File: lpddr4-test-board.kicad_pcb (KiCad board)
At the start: 8 copper layers, 117 x 86 mm, 257 parts, among them IC1 TPS54561, IC3 TPD8S009DSMR, J1 0878311420, J10 61300311121, J2 08B0-1X1T-36-F, J3 DC_SOCKET, J4 WE_629105150521, J5 2309409-1, J6 685119134923, J7 1140084168, Q2 BSS138APW, Q3 BSS138APW, Q4 BSS138APW, Q5 BSS138APW, Q6 BSS138APW, Q7 BSS138APW, Q8 BSS138APW, U1 XC7K70T-FBG484, U2 ASEM1-100.000MHZ-LC-T, U3 S25FL128SAGNFI000, U4 TPS65296, U5 TPS62823DLCT, U6 DP83848JSQ_NOPB, U7 FT4232HQ, Y1 ABM8G-25.000MHZ-18-D2Y-T

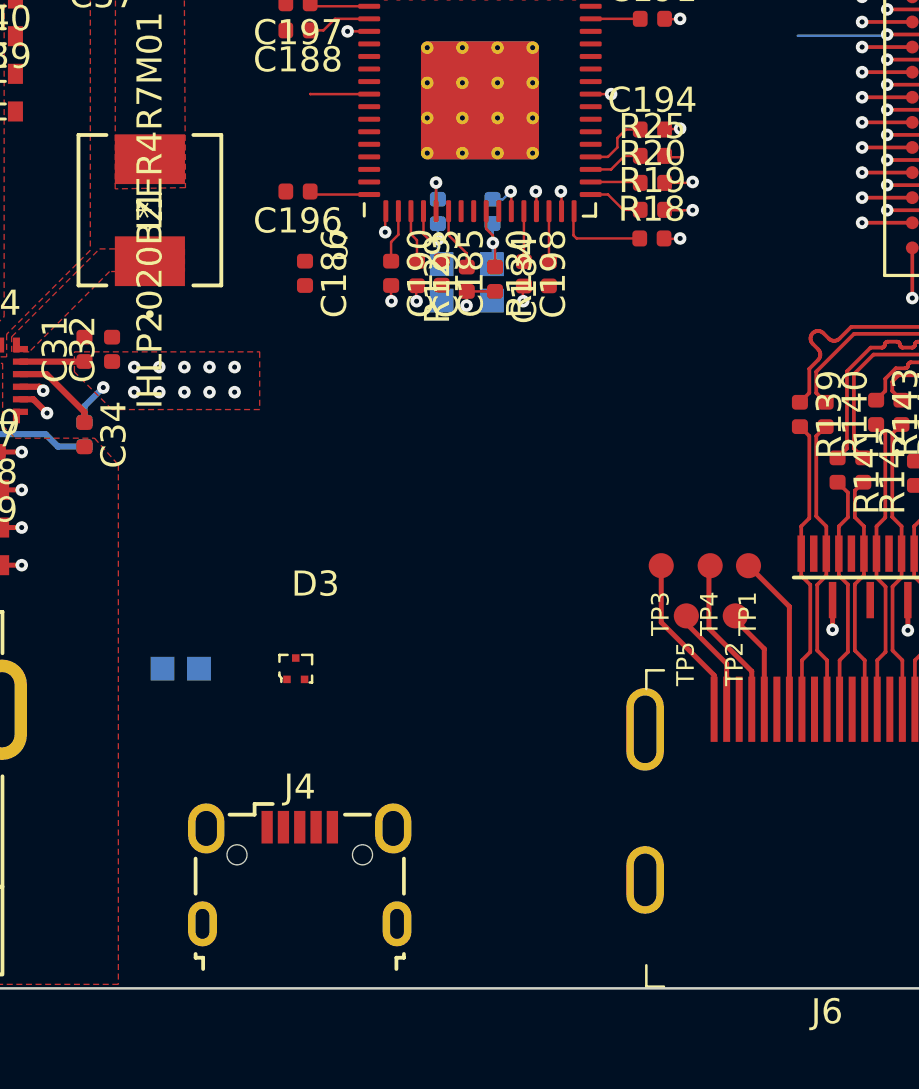
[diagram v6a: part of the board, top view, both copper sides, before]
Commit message: Add aux JTAG connection to schematics
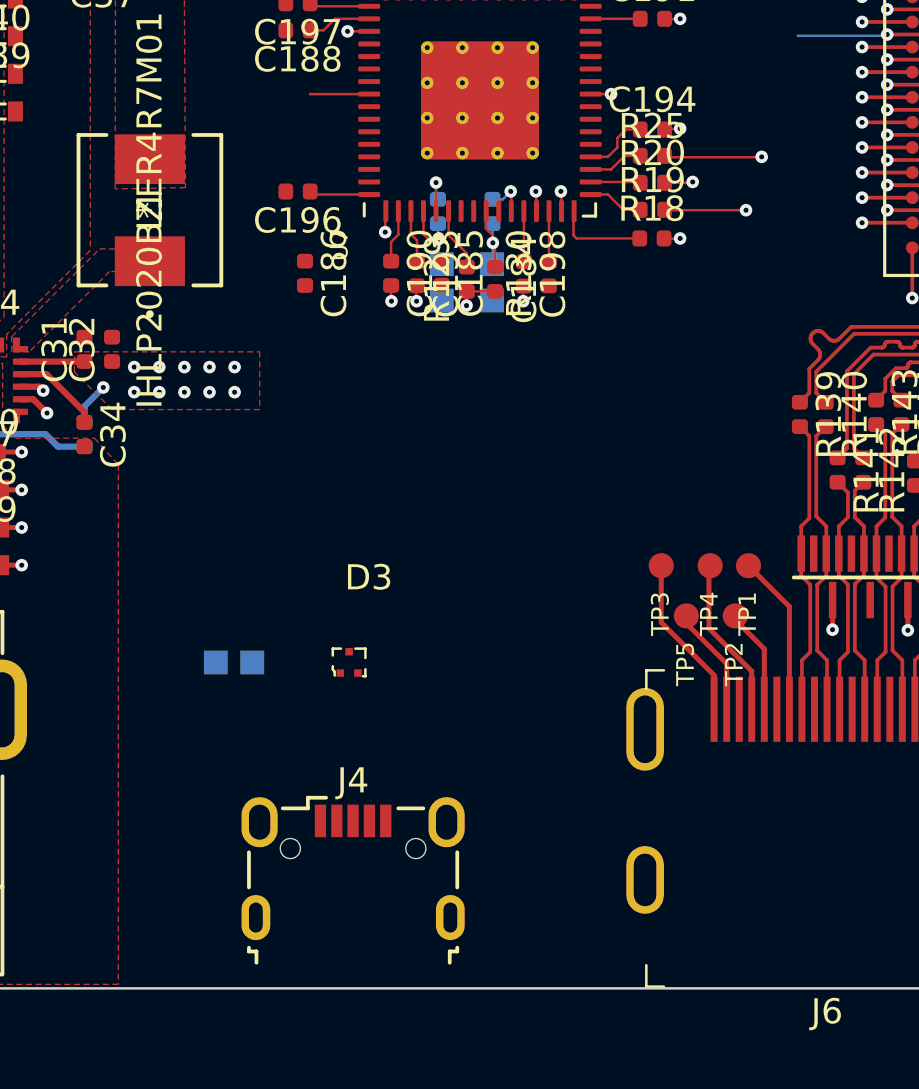
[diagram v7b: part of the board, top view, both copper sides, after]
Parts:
- moved D3 2.14 mm to (136.1, 123.0)
- moved FB6 2.14 mm to (131.5, 123.0)
- moved J4 2.14 mm to (136.3, 131.2)
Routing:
- net TCK_JTAG: track 76.5 -> 90.1 mm
- net TDI_JTAG: track 79.8 -> 90.7 mm
- net TDO_JTAG: track 80.2 -> 88.6 mm
- net TMS_JTAG: track 79.6 -> 86.7 mm
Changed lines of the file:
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@@
     (thickness 1.6)
     (drawings 130)
-    (tracks 3158)
+    (tracks 3169)
     (zones 0)
     (modules 257)
@@
   )
   (module lpddr4-test-board-footprints:0603 (layer B.Cu)
-    (at 129.389 123.264)
+    (at 131.514 123.014)
     (attr smd)
     (fp_text reference FB6 (at 0 0 90) (layer F.SilkS) hide
@@
   )
   (module lpddr4-test-board-footprints:SOT-3 (layer F.Cu)
-    (at 133.97281 123.264)
+    (at 136.09781 123.014)
     (descr http://www.ti.com/lit/ds/symlink/tpd2eusb30.pdf)
     (attr smd)
@@
   )
   (module lpddr4-test-board-footprints:USB_Micro_B_Female_629105150521 (layer F.Cu)
-    (at 134.132 131.479)
+    (at 136.257 131.229)
     (descr "USB Micro-B receptacle, http://www.mouser.com/ds/2/445/629105150521-469306.pdf")
     (tags "usb micro receptacle")
@@
   (segment (start 170.411328 90.997157) (end 171.036329 90.997156) (width 0.1) (layer In5.Cu) (net 23))
   (segment (start 168.620327 89.247157) (end 170.370327 90.997157) (width 0.1) (layer In5.Cu) (net 23))
-  (segment (start 148.786328 89.247157) (end 168.620327 89.247157) (width 0.1) (layer In5.Cu) (net 23))
   (segment (start 170.370327 90.997157) (end 170.411328 90.997157) (width 0.1) (layer In5.Cu) (net 23))
-  (segment (start 149.286328 106.122157) (end 149.286328 106.747157) (width 0.1) (layer In5.Cu) (net 23))
-  (via blind (at 149.286328 102.872157) (size 0.5) (drill 0.2) (layers GND1 In5.Cu) (net 24))
-  (segment (start 148.661328 102.887157) (end 149.271328 102.887157) (width 0.1) (layer F.Cu) (net 24))
+  (segment (start 157.536328 89.247157) (end 156.036328 89.247157) (width 0.1) (layer In5.Cu) (net 23))
+  (segment (start 157.536328 89.247157) (end 168.620327 89.247157) (width 0.1) (layer In5.Cu) (net 23))
+  (segment (start 156.036328 89.247157) (end 153.161328 92.122157) (width 0.1) (layer In5.Cu) (net 23))
+  (segment (start 153.161328 92.122157) (end 153.161328 104.997157) (width 0.1) (layer In5.Cu) (net 23))
+  (segment (start 149.286328 106.122157) (end 152.036328 106.122157) (width 0.1) (layer In5.Cu) (net 23))
+  (segment (start 153.161328 104.997157) (end 152.036328 106.122157) (width 0.1) (layer In5.Cu) (net 23))
+  (segment (start 157.286328 89.247157) (end 157.536328 89.247157) (width 0.1) (layer In5.Cu) (net 23))
   (segment (start 169.536329 90.497157) (end 170.036329 89.997157) (width 0.15) (layer F.Cu) (net 24))
   (via blind (at 170.036329 89.997157) (size 0.5) (drill 0.2) (layers F.Cu In5.Cu) (net 24) (status 40000))
@@
   (segment (start 206.278 72.273) (end 203.323 72.273) (width 0.15) (layer F.Cu) (net 24))
   (segment (start 195.981 77.123) (end 201.95 77.123) (width 0.1) (layer In2.Cu) (net 24))
-  (segment (start 149.286328 105.372157) (end 149.286328 102.872157) (width 0.1) (layer In5.Cu) (net 24))
-  (segment (start 169.036328 88.997157) (end 148.598828 88.997157) (width 0.1) (layer In5.Cu) (net 24))
-  (segment (start 149.786328 105.872157) (end 149.286328 105.372157) (width 0.1) (layer In5.Cu) (net 24))
+  (segment (start 148.661328 102.887157) (end 152.521328 102.887157) (width 0.1) (layer F.Cu) (net 24))
+  (via blind (at 152.536328 102.872157) (size 0.5) (drill 0.2) (layers F.Cu In5.Cu) (net 24))
+  (segment (start 152.521328 102.887157) (end 152.536328 102.872157) (width 0.1) (layer F.Cu) (net 24))
+  (segment (start 152.911328 91.997157) (end 152.911328 102.497157) (width 0.1) (layer In5.Cu) (net 24))
+  (segment (start 152.911328 102.497157) (end 152.536328 102.872157) (width 0.1) (layer In5.Cu) (net 24))
+  (segment (start 155.911328 88.997157) (end 152.911328 91.997157) (width 0.1) (layer In5.Cu) (net 24))
+  (segment (start 169.036328 88.997157) (end 155.911328 88.997157) (width 0.1) (layer In5.Cu) (net 24))
   (segment (start 170.036329 89.997157) (end 170.036328 89.997157) (width 0.1) (layer In5.Cu) (net 24))
   (segment (start 170.036328 89.997157) (end 169.036328 88.997157) (width 0.1) (layer In5.Cu) (net 24))
-  (segment (start 149.786328 106.809657) (end 149.786328 105.872157) (width 0.1) (layer In5.Cu) (net 24))
   (segment (start 170.536329 90.497156) (end 171.036329 89.997156) (width 0.15) (layer F.Cu) (net 25))
   (via blind (at 171.036329 89.997156) (size 0.5) (drill 0.2) (layers F.Cu In5.Cu) (net 25) (status 40000))
@@
   (segment (start 182.9 89.061) (end 196.235 75.726) (width 0.1) (layer In2.Cu) (net 25))
   (segment (start 196.235 75.726) (end 201.061 75.726) (width 0.1) (layer In2.Cu) (net 25))
+  (via blind (at 151.911328 104.997157) (size 0.5) (drill 0.2) (layers F.Cu In5.Cu) (net 25))
+  (segment (start 148.676328 104.997157) (end 151.911328 104.997157) (width 0.1) (layer F.Cu) (net 25))
   (segment (start 148.661328 105.012157) (end 148.676328 104.997157) (width 0.1) (layer F.Cu) (net 25))
-  (segment (start 148.676328 104.997157) (end 149.432775 104.997157) (width 0.1) (layer F.Cu) (net 25))
-  (segment (start 149.432775 104.997157) (end 149.786328 104.997157) (width 0.1) (layer F.Cu) (net 25))
-  (via blind (at 149.786328 104.997157) (size 0.5) (drill 0.2) (layers F.Cu In5.Cu) (net 25))
-  (segment (start 150.036327 105.247156) (end 149.786328 104.997157) (width 0.1) (layer In5.Cu) (net 25))
-  (segment (start 150.036328 106.70609) (end 150.036327 105.247156) (width 0.1) (layer In5.Cu) (net 25))
-  (segment (start 169.432766 88.747146) (end 148.495271 88.747147) (width 0.1) (layer In5.Cu) (net 25))
   (segment (start 170.682776 89.997156) (end 169.432766 88.747146) (width 0.1) (layer In5.Cu) (net 25))
+  (segment (start 152.661328 91.872157) (end 152.661328 101.997157) (width 0.1) (layer In5.Cu) (net 25))
   (segment (start 171.036329 89.997156) (end 170.682776 89.997156) (width 0.1) (layer In5.Cu) (net 25))
+  (segment (start 152.036328 102.622157) (end 152.036328 104.872157) (width 0.1) (layer In5.Cu) (net 25))
+  (segment (start 155.786339 88.747146) (end 152.661328 91.872157) (width 0.1) (layer In5.Cu) (net 25))
+  (segment (start 152.036328 104.872157) (end 151.911328 104.997157) (width 0.1) (layer In5.Cu) (net 25))
+  (segment (start 169.432766 88.747146) (end 155.786339 88.747146) (width 0.1) (layer In5.Cu) (net 25))
+  (segment (start 152.661328 101.997157) (end 152.036328 102.622157) (width 0.1) (layer In5.Cu) (net 25))
   (segment (start 171.536329 90.497156) (end 172.036329 89.997157) (width 0.15) (layer F.Cu) (net 26))
   (via blind (at 172.036329 89.997157) (size 0.5) (drill 0.2) (layers F.Cu In5.Cu) (net 26) (status 40000))
@@
   (segment (start 148.666328 103.907157) (end 149.751328 103.907157) (width 0.1) (layer F.Cu) (net 26))
   (via blind (at 149.786328 103.872157) (size 0.5) (drill 0.2) (layers F.Cu In5.Cu) (net 26))
-  (segment (start 150.036327 104.122156) (end 149.786328 103.872157) (width 0.1) (layer In5.Cu) (net 26))
-  (segment (start 150.286328 104.372157) (end 150.036327 104.122156) (width 0.1) (layer In5.Cu) (net 26))
-  (segment (start 150.286328 106.497157) (end 150.286328 104.372157) (width 0.1) (layer In5.Cu) (net 26))
-  (segment (start 171.48633 89.447158) (end 170.589897 89.447158) (width 0.1) (layer In5.Cu) (net 26))
-  (segment (start 170.589897 89.447158) (end 169.639874 88.497135) (width 0.1) (layer In5.Cu) (net 26))
+  (segment (start 151.661328 103.497157) (end 151.286328 103.872157) (width 0.1) (layer In5.Cu) (net 26))
+  (segment (start 151.661328 102.497157) (end 151.661328 103.497157) (width 0.1) (layer In5.Cu) (net 26))
+  (segment (start 151.286328 103.872157) (end 149.786328 103.872157) (width 0.1) (layer In5.Cu) (net 26))
+  (segment (start 152.411318 101.747167) (end 151.661328 102.497157) (width 0.1) (layer In5.Cu) (net 26))
   (segment (start 172.036329 89.997157) (end 171.48633 89.447158) (width 0.1) (layer In5.Cu) (net 26))
-  (segment (start 169.639874 88.497135) (end 148.28635 88.497135) (width 0.1) (layer In5.Cu) (net 26))
+  (segment (start 155.682782 88.497136) (end 152.411318 91.7686) (width 0.1) (layer In5.Cu) (net 26))
+  (segment (start 170.589897 89.447158) (end 169.639874 88.497135) (width 0.1) (layer In5.Cu) (net 26))
+  (segment (start 169.639874 88.497135) (end 155.682782 88.497136) (width 0.1) (layer In5.Cu) (net 26))
+  (segment (start 171.48633 89.447158) (end 170.589897 89.447158) (width 0.1) (layer In5.Cu) (net 26))
+  (segment (start 152.411318 91.7686) (end 152.411318 101.747167) (width 0.1) (layer In5.Cu) (net 26))
   (segment (start 205.00001 101.93499) (end 205.465 101.47) (width 0.1) (layer B.Cu) (net 27))
   (segment (start 205.00001 107.82199) (end 205.00001 101.93499) (width 0.1) (layer B.Cu) (net 27))

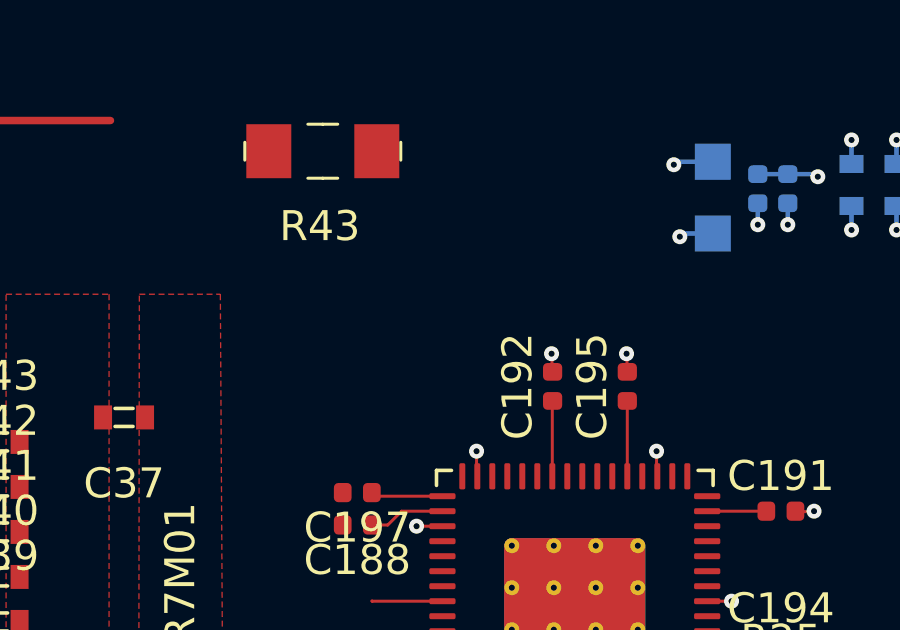
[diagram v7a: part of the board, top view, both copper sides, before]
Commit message: Import JTAG-related components to PCB
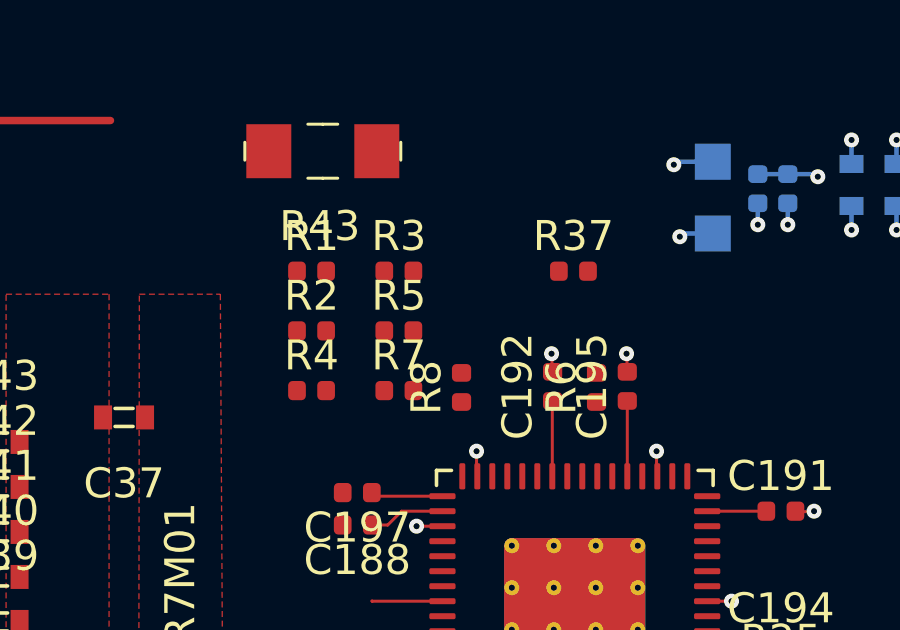
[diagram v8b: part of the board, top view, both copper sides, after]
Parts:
- added R1: R_22R_0402, antmicro-footprints:0402-res, F.Cu at (132.5, 89.4)
- added R2: R_22R_0402, antmicro-footprints:0402-res, F.Cu at (132.5, 91.4)
- added R3: R_22R_0402, antmicro-footprints:0402-res, F.Cu at (135.4, 89.4)
- added R37: R_22R_0402, antmicro-footprints:0402-res, F.Cu at (141.3, 89.4)
- added R4: R_22R_0402, antmicro-footprints:0402-res, F.Cu at (132.5, 93.4)
- added R5: R_22R_0402, antmicro-footprints:0402-res, F.Cu at (135.4, 91.4)
- added R6: R_22R_0402, antmicro-footprints:0402-res, F.Cu at (142.0, 93.2)
- added R7: R_22R_0402, antmicro-footprints:0402-res, F.Cu at (135.4, 93.4)
- added R8: R_22R_0402, antmicro-footprints:0402-res, F.Cu at (137.5, 93.2)
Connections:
- J5 pad 1: Net-(J5-Pad1) -> GND
- J5 pad 10: Net-(J5-Pad10) -> GND
- J5 pad 11: Net-(J5-Pad11) -> GND
- J5 pad 115: Net-(J5-Pad115) -> VDD2
- J5 pad 116: Net-(J5-Pad116) -> VDD1
- J5 pad 117: Net-(J5-Pad117) -> VDD2
- J5 pad 118: Net-(J5-Pad118) -> VDD1
- J5 pad 119: Net-(J5-Pad119) -> VDD2
- J5 pad 12: Net-(J5-Pad12) -> GND
- J5 pad 120: Net-(J5-Pad120) -> VDD1
- J5 pad 121: Net-(J5-Pad121) -> VDD2
- J5 pad 122: Net-(J5-Pad122) -> VDD1
- J5 pad 123: Net-(J5-Pad123) -> VDD2
- J5 pad 124: Net-(J5-Pad124) -> VDD1
- J5 pad 125: Net-(J5-Pad125) -> VDD2
- J5 pad 126: Net-(J5-Pad126) -> VDDQ
- J5 pad 127: Net-(J5-Pad127) -> VDD2
- J5 pad 128: Net-(J5-Pad128) -> VDDQ
- J5 pad 129: Net-(J5-Pad129) -> VDD2
- J5 pad 13: Net-(J5-Pad13) -> GND
- J5 pad 130: Net-(J5-Pad130) -> VDDQ
- J5 pad 14: Net-(J5-Pad14) -> GND
- J5 pad 15: Net-(J5-Pad15) -> GND
- J5 pad 16: Net-(J5-Pad16) -> GND
- J5 pad 17: Net-(J5-Pad17) -> GND
- J5 pad 18: Net-(J5-Pad18) -> GND
- J5 pad 19: Net-(J5-Pad19) -> GND
- J5 pad 2: Net-(J5-Pad2) -> GND
- J5 pad 20: Net-(J5-Pad20) -> GND
- J5 pad 21: Net-(J5-Pad21) -> GND
- J5 pad 22: Net-(J5-Pad22) -> GND
- J5 pad 23: Net-(J5-Pad23) -> GND
- J5 pad 24: Net-(J5-Pad24) -> GND
- J5 pad 245: Net-(J5-Pad245) -> VDD2
- J5 pad 246: Net-(J5-Pad246) -> VDDQ
- J5 pad 247: Net-(J5-Pad247) -> VDD2
- J5 pad 248: Net-(J5-Pad248) -> VDDQ
- J5 pad 249: Net-(J5-Pad249) -> VDD2
- J5 pad 25: Net-(J5-Pad25) -> GND
- J5 pad 250: Net-(J5-Pad250) -> VDDQ
- J5 pad 251: Net-(J5-Pad251) -> VDD2
- J5 pad 252: Net-(J5-Pad252) -> VDD1
- J5 pad 253: Net-(J5-Pad253) -> VDD2
- J5 pad 254: Net-(J5-Pad254) -> VDD1
- J5 pad 255: Net-(J5-Pad255) -> VDD2
- J5 pad 256: Net-(J5-Pad256) -> VDD1
- J5 pad 257: Net-(J5-Pad257) -> VDD2
- J5 pad 258: Net-(J5-Pad258) -> VDD1
- J5 pad 259: Net-(J5-Pad259) -> VDD2
- J5 pad 26: Net-(J5-Pad26) -> GND
- J5 pad 260: Net-(J5-Pad260) -> VDD1
- J5 pad 27: Net-(J5-Pad27) -> GND
- J5 pad 28: Net-(J5-Pad28) -> GND
- J5 pad 29: Net-(J5-Pad29) -> GND
- J5 pad 3: Net-(J5-Pad3) -> GND
- J5 pad 30: Net-(J5-Pad30) -> GND
- J5 pad 31: Net-(J5-Pad31) -> GND
- J5 pad 32: Net-(J5-Pad32) -> GND
- J5 pad 33: Net-(J5-Pad33) -> GND
- J5 pad 34: Net-(J5-Pad34) -> GND
- J5 pad 35: Net-(J5-Pad35) -> GND
- J5 pad 36: Net-(J5-Pad36) -> GND
- J5 pad 37: Net-(J5-Pad37) -> GND
- J5 pad 38: Net-(J5-Pad38) -> GND
- J5 pad 39: Net-(J5-Pad39) -> GND
- J5 pad 4: Net-(J5-Pad4) -> GND
- J5 pad 40: Net-(J5-Pad40) -> GND
- J5 pad 41: Net-(J5-Pad41) -> GND
- J5 pad 42: Net-(J5-Pad42) -> GND
- J5 pad 43: Net-(J5-Pad43) -> GND
- J5 pad 44: Net-(J5-Pad44) -> GND
- J5 pad 45: Net-(J5-Pad45) -> GND
- J5 pad 46: Net-(J5-Pad46) -> GND
- J5 pad 47: Net-(J5-Pad47) -> GND
- J5 pad 48: Net-(J5-Pad48) -> GND
- J5 pad 49: Net-(J5-Pad49) -> GND
- J5 pad 5: Net-(J5-Pad5) -> GND
- J5 pad 50: Net-(J5-Pad50) -> GND
- J5 pad 6: Net-(J5-Pad6) -> GND
- J5 pad 7: Net-(J5-Pad7) -> GND
- J5 pad 8: Net-(J5-Pad8) -> GND
- J5 pad 9: Net-(J5-Pad9) -> GND
- J5 pad S1: Net-(J5-PadS1) -> GND
- J5 pad S2: Net-(J5-PadS1) -> GND
